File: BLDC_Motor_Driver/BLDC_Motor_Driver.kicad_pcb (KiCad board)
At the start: 4 copper layers, 139 parts, among them J101 Conn_01x08, J102 395221002, J103 USB4105-GF-A, J104 Conn_01x05, J105 Conn_01x05, J106 Conn_01x04, J107 395221005, J108 395221003, J109 Conn_02x12_Counter_Clockwise, J110 395221005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

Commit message: move elements to logical regions
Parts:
- J101: value Conn_01x08 -> Conn_01x10; footprint Connector_PinHeader_2.54mm:PinHeader_1x08_P2.54mm_Vertical -> Connector_PinHeader_2.54mm:PinHeader_1x10_P2.54mm_Vertical
- U302: footprint Package_SO:HSOP-8-1EP_3.9x4.9mm_P1.27mm_EP2.41x3.1mm -> Package_SO:HSOP-8-1EP_3.9x4.9mm_P1.27mm_EP2.41x3.1mm_ThermalVias
- moved J107 249.3 mm to (273.0, 77.5), turned to 90 degrees
- moved C101 241.6 mm to (267.6, 77.7), turned to 180 degrees
- moved C308 229.4 mm to (250.1, 137.9), turned to 180 degrees
- moved C307 229.3 mm to (252.0, 50.0), turned to 180 degrees
- moved J108 219.3 mm to (273.0, 104.0), turned to 90 degrees
- moved D302 217.4 mm to (248.0, 34.5), turned to 180 degrees
- moved J102 203.9 mm to (250.5, 27.0), turned to 180 degrees
- moved J110 200.3 mm to (193.5, 150.0)
- moved C103 190.3 mm to (193.5, 144.9), turned to 90 degrees
- moved C504 185.6 mm to (261.6, 96.4)
- moved C502 185.2 mm to (261.6, 92.9)
- moved C702 180.1 mm to (250.1, 122.9)
- moved C703 180.1 mm to (250.9, 119.6)
- moved C704 180.1 mm to (250.1, 125.5)
- moved C701 180.1 mm to (254.3, 123.2)
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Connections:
- J101 pad 2: /Gate-Driver/GPIO0 -> /Gate-Driver/ENC_B
- J101 pad 3: /Gate-Driver/GPIO1 -> /Gate-Driver/ENC_N
- J101 pad 4: /Gate-Driver/GPIO5 -> /Gate-Driver/GPIO0
- J101 pad 5: /Gate-Driver/GPIO15 -> /Gate-Driver/GPIO1
- J101 pad 6: /Gate-Driver/GPIO16 -> /Gate-Driver/GPIO5
- J101 pad 7: /Gate-Driver/GPIO17 -> /Gate-Driver/GPIO15
- J101 pad 8: /Gate-Driver/GPIO18 -> /Gate-Driver/GPIO16
- J103 pad A6: /D- -> /D+
- J103 pad A7: /D+ -> /D-
- J103 pad B6: /D- -> /D+
- J103 pad B7: /D+ -> /D-
- U101 pad 1: /USB_D+ -> /D+
- U101 pad 2: /USB_D- -> /D-
- U101 pad 5: /D- -> /USB_D-
- U101 pad 6: /D+ -> /USB_D+

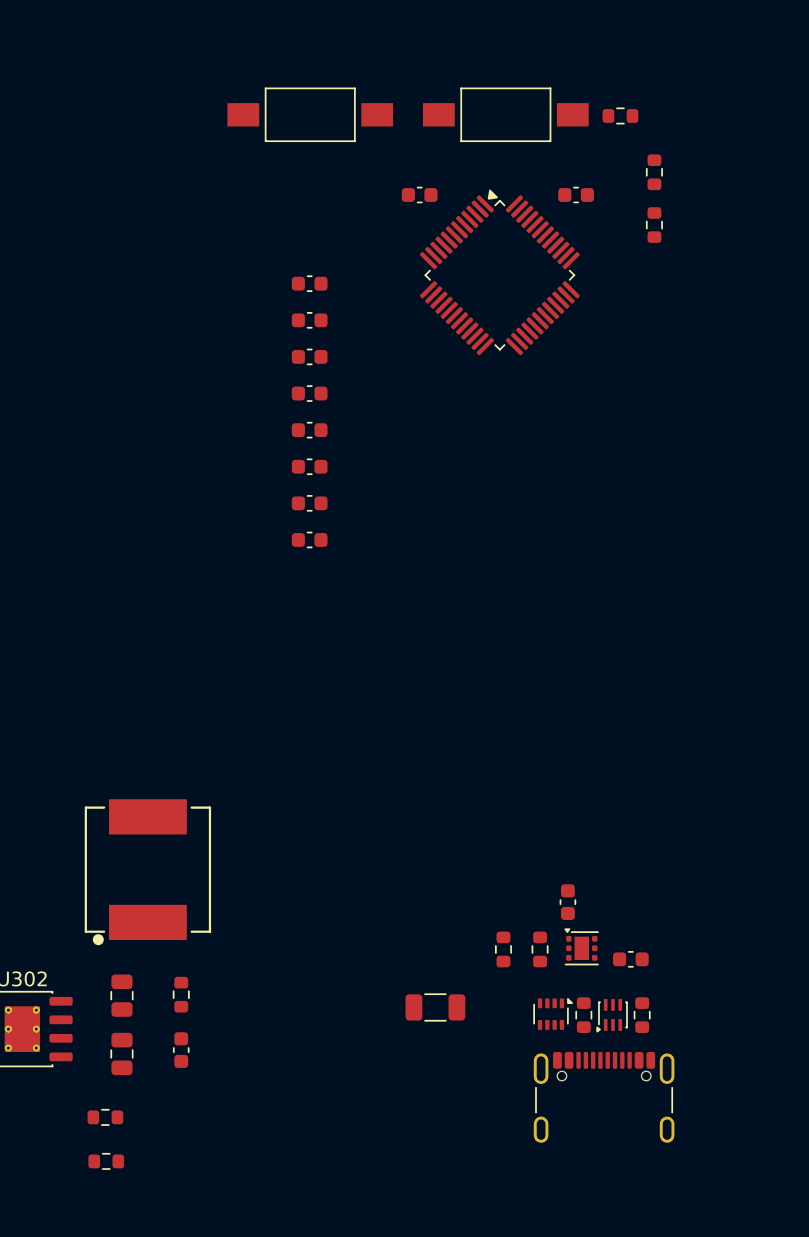
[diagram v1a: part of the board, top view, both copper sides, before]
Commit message: aligned MCU and USB components
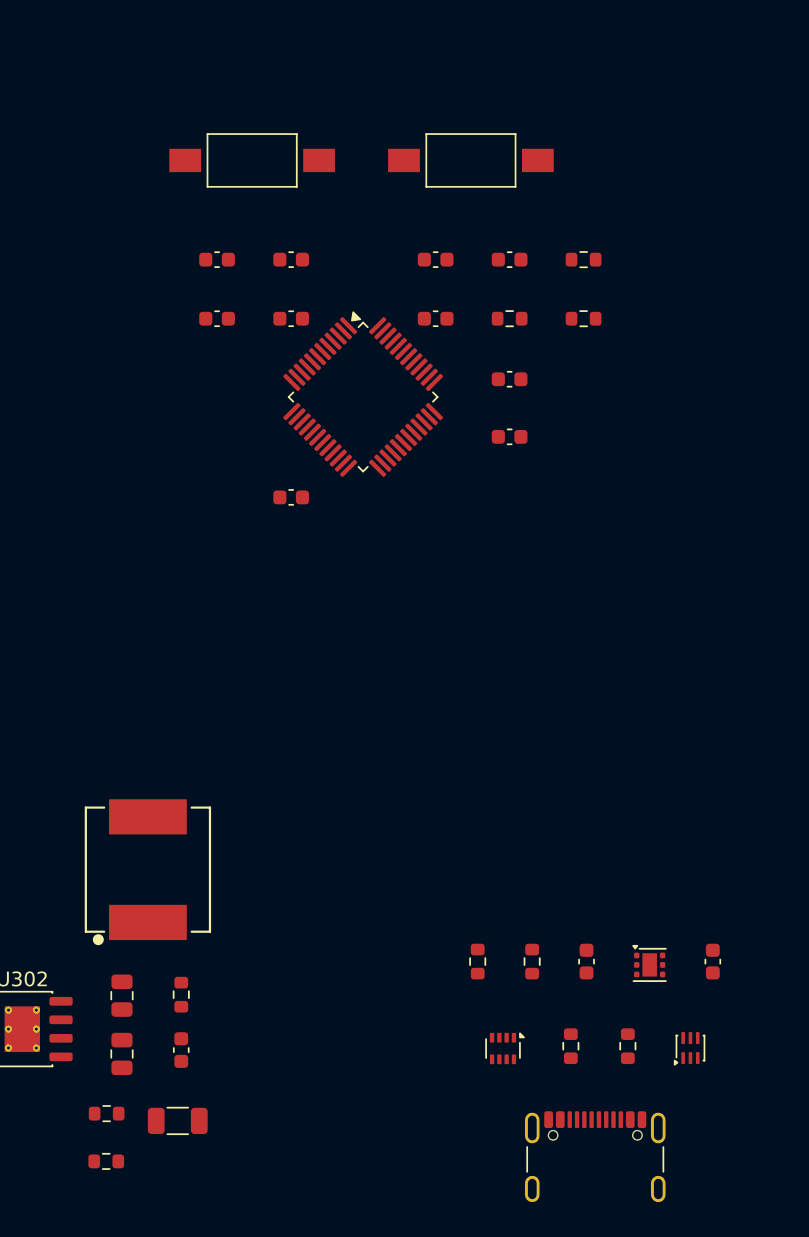
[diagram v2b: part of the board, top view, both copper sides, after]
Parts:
- moved C208 21.1 mm to (148.8, 96.3)
- moved C309 19.3 mm to (131.2, 155.4)
- moved C207 14.4 mm to (153.9, 108.5)
- moved R401 14.1 mm to (153.9, 100.4), turned to 180 degrees
- moved C204 13.7 mm to (153.9, 104.5)
- moved U201 12.6 mm to (143.9, 105.8)
- moved C104 12.2 mm to (138.9, 100.4)
- moved C202 12.2 mm to (138.9, 112.7), turned to 180 degrees
- moved C206 12.0 mm to (133.8, 100.4), turned to 180 degrees
- moved C205 11.8 mm to (138.9, 96.3), turned to 180 degrees
- moved R107 10.2 mm to (159.0, 96.3)
- moved C203 9.02 mm to (148.8, 100.4)
- moved R402 8.05 mm to (159.0, 100.4), turned to 180 degrees
- moved C201 6.56 mm to (133.8, 96.3), turned to 180 degrees
- moved C102 6.36 mm to (153.9, 96.3)
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
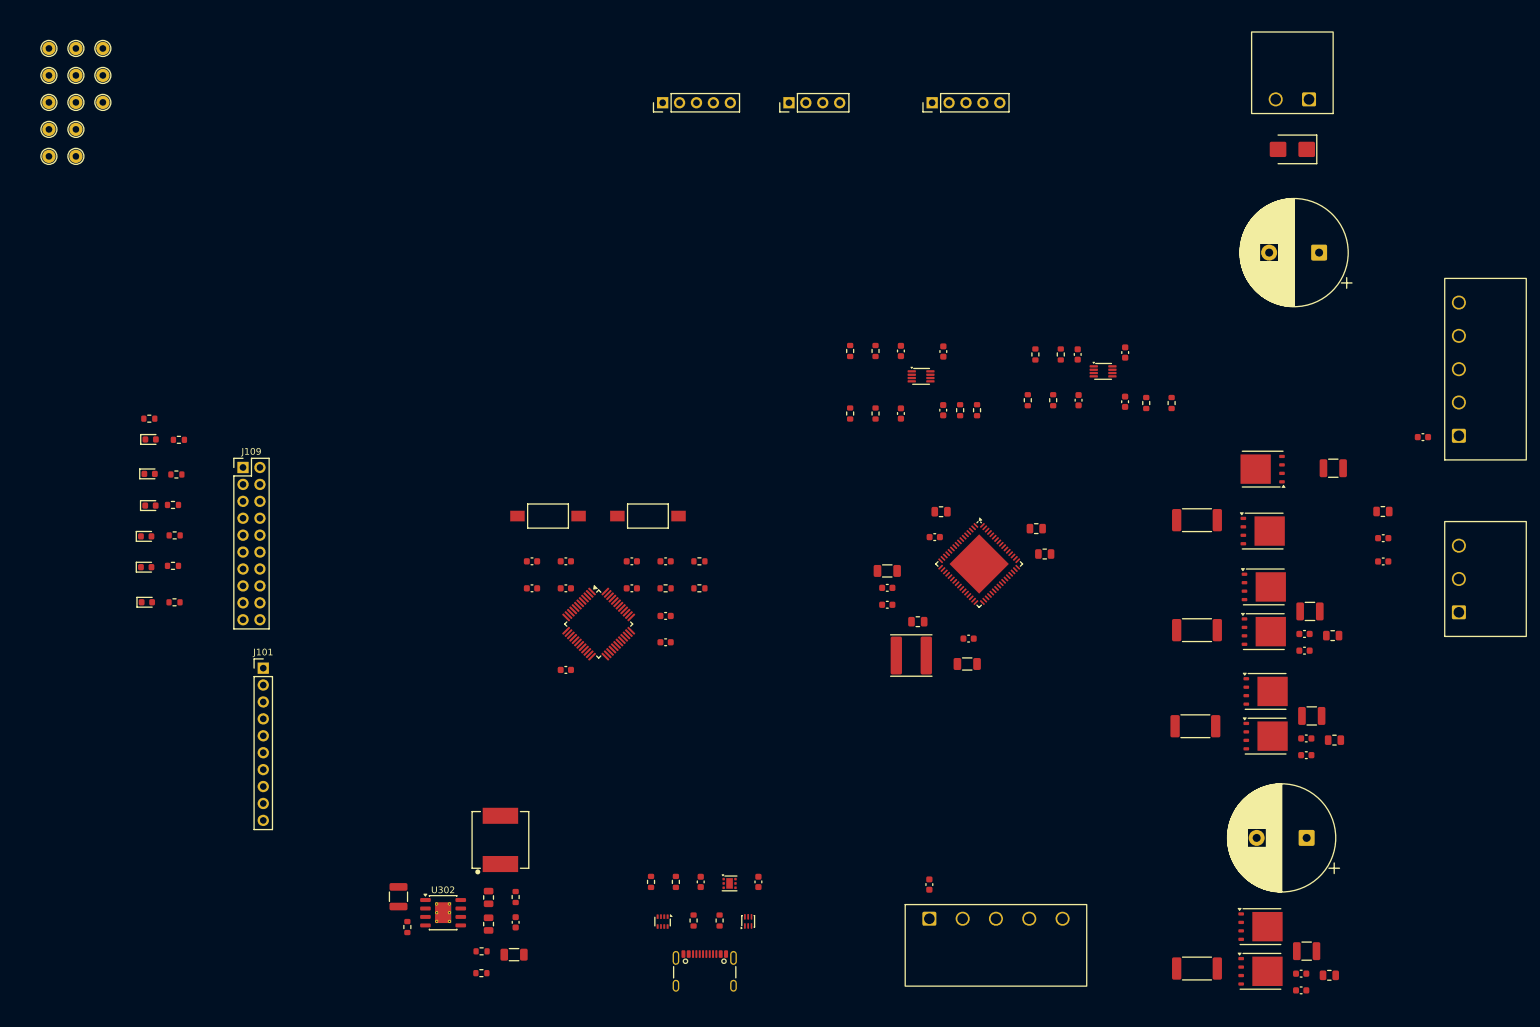
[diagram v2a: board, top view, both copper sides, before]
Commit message: complete top-layer routing for MCU, G_DRV, USB_PWR, HALL areas
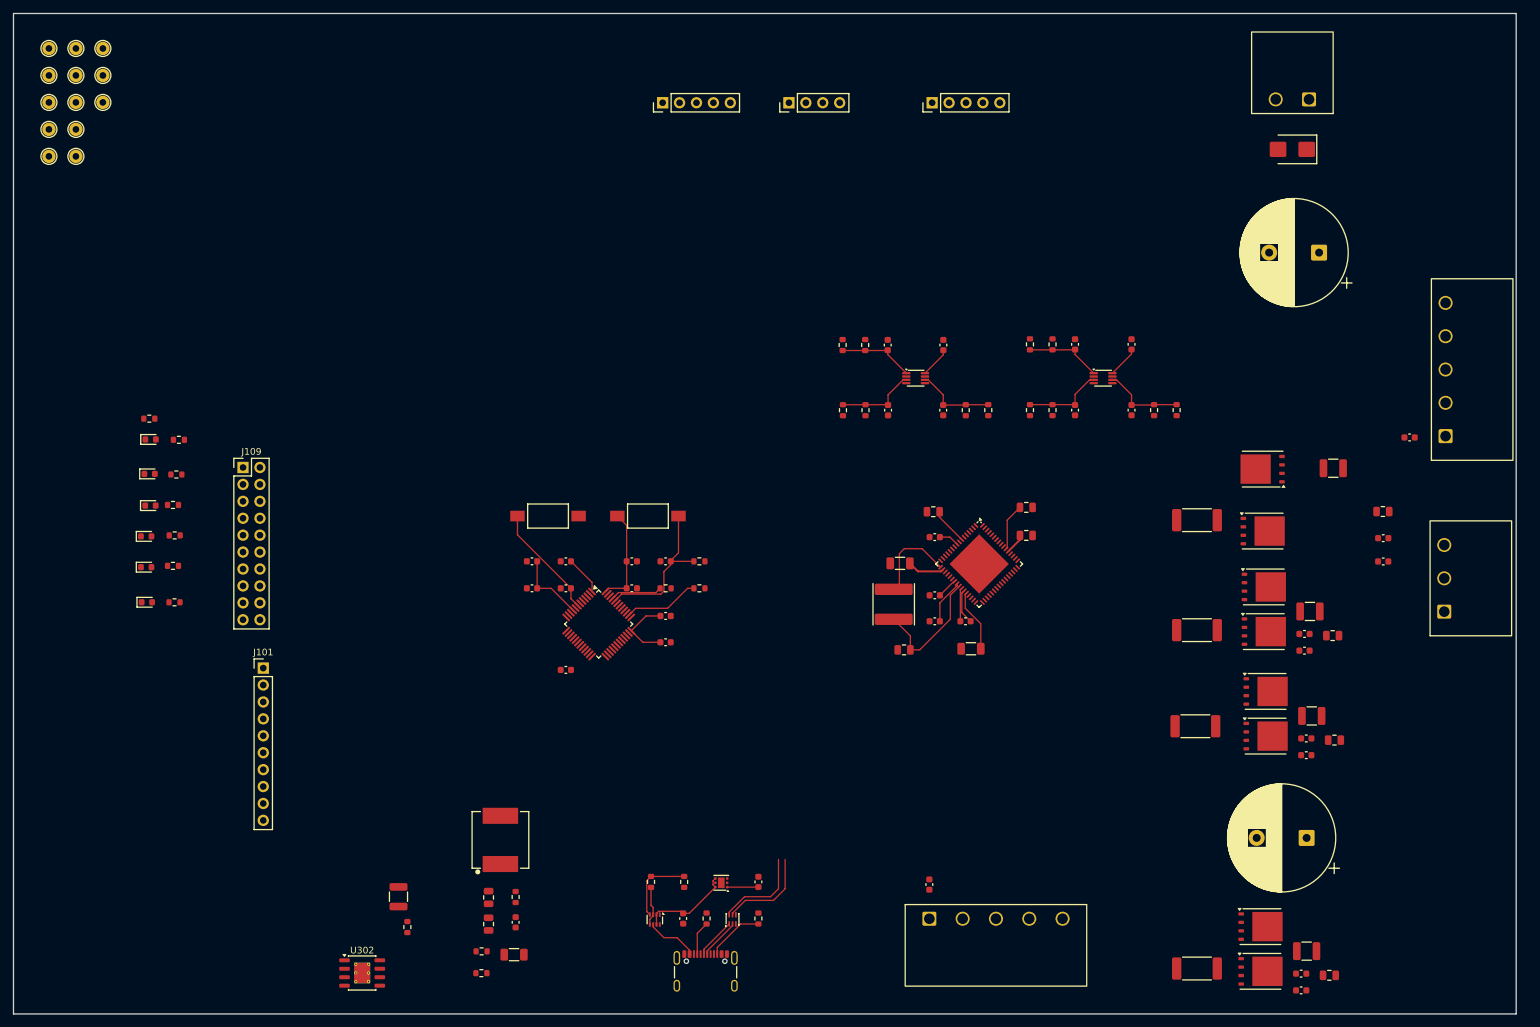
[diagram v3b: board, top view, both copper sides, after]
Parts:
- moved U302 15.2 mm to (108.3, 158.2)
- moved C302 12.6 mm to (156.5, 150.0), turned to -90 degrees
- moved C303 8.66 mm to (167.8, 144.5)
- moved L401 8.13 mm to (188.2, 102.8), turned to -90 degrees
- moved C410 7.54 mm to (194.3, 105.3)
- moved C409 7.21 mm to (194.3, 101.5)
- moved R106 5.83 mm to (167.8, 150.0)
- moved C402 4.71 mm to (189.7, 109.6)
- moved C405 3.93 mm to (208.1, 92.5)
- moved C407 3.53 mm to (208.1, 88.2)
- moved C401 2.64 mm to (198.9, 105.3)
- moved U101 2.37 mm to (164.0, 150.1)
- moved C408 2.36 mm to (199.7, 109.5)
- moved C406 2.23 mm to (189.1, 96.7)
- moved J108 2.20 mm to (270.8, 103.9)
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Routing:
- net +3V3: track 0.00 -> 49.6 mm
- net /BOOT0: track 0.00 -> 23.6 mm
- net /DRIVER_V_{BUCK}: track 0.00 -> 19.1 mm
- net /NRST: track 0.00 -> 17.2 mm
- net /USB_D-: track 0.00 -> 14.1 mm
- net /5V_COM: track 0.00 -> 14.0 mm
- net /USB_D+: track 0.00 -> 13.7 mm
- net /Gate-Driver/DRIVER_SW: track 0.00 -> 13.4 mm
- net /5V_DRV: track 0.00 -> 12.4 mm
- net Net-(U402-3A): track 0.00 -> 12.1 mm
- net Net-(U402-2A): track 0.00 -> 12.1 mm
- net Net-(U403-3A): track 0.00 -> 12.0 mm
- net Net-(U403-2A): track 0.00 -> 12.0 mm
- net Net-(U402-1A): track 0.00 -> 11.9 mm
- net /DRIVER_RSTN: track 0.00 -> 11.4 mm
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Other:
- board outline added: 225.6 x 150.2 mm

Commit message: used external tool to duplicate half-bridge layouts. updated gitignore. redoing gate driver layout with high-side mosfet bootstrap caps
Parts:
- removed C801: 100nF, Capacitor_SMD:C_0805_2012Metric
- removed C802: 1nF, Capacitor_SMD:C_0603_1608Metric
- removed C803: 4.7uF, Capacitor_SMD:C_1210_3225Metric
- removed C804: 1uF, Capacitor_SMD:C_0603_1608Metric
- removed Q801, Q802: CSD18540Q5B, Package_TO_SOT_SMD:TDSON-8-1
- removed R801: 3mΩ, Resistor_SMD:R_2512_6332Metric_Pad1.40x3.35mm_HandSolder
- moved C504 52.6 mm to (209.2, 92.7)
- moved C704 46.2 mm to (209.3, 103.7), turned to 180 degrees
- moved C604 41.7 mm to (209.3, 99.9), turned to 180 degrees
- moved C701 32.2 mm to (224.1, 112.1)
- moved C703 29.3 mm to (223.5, 109.3)
- moved C307 25.7 mm to (263.5, 27.0), turned to 0 degrees
- moved C501 20.7 mm to (241.7, 83.2)
- moved Q701 19.9 mm to (224.3, 119.1), turned to 180 degrees
- moved R501 17.0 mm to (247.7, 80.7)
- moved R601 16.2 mm to (248.3, 99.6)
- moved C702 14.9 mm to (236.6, 116.6), turned to 90 degrees
- moved C503 13.2 mm to (241.1, 80.3)
- moved C601 13.0 mm to (242.2, 102.1)
- moved Q702 12.1 mm to (232.6, 118.7), turned to -90 degrees
- moved R701 12.0 mm to (230.2, 109.6)
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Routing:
- net /DRIVER_V_{BUCK}: track 19.1 -> 0.00 mm
- net GND: track 0.00 -> 18.8 mm
- net /Gate-Driver/DRIVER_SW: track 13.4 -> 0.00 mm
- net /Gate-Driver/DRIVER_V_{DRV}: track 9.39 -> 0.00 mm
- net /Gate-Driver/BS_W: track 0.00 -> 7.65 mm
- net /DRIVER_V_{EXT2}: track 6.71 -> 0.00 mm
- net /Gate-Driver/BS_V: track 0.00 -> 6.59 mm
- net /MOTOR_W: track 0.00 -> 6.52 mm
- net /Gate-Driver/CSP_U: track 0.00 -> 5.59 mm
- net /Gate-Driver/CSP_W: track 0.00 -> 5.59 mm
- net /Gate-Driver/CSP_V: track 0.00 -> 5.59 mm
- net +1V8: track 5.56 -> 0.00 mm
- net /Gate-Driver/DRIVER_CPI: track 5.27 -> 0.00 mm
- net /Gate-Driver/DRIVER_CPO: track 5.03 -> 0.00 mm
- net /MOTOR_U: track 0.00 -> 4.88 mm
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- added copper zone on F.Cu, net (none)
- added copper zone on F.Cu, net +36V
- added copper zone on F.Cu, net /Gate-Driver/CSP_U
- added copper zone on F.Cu, net /Gate-Driver/CSP_V
- added copper zone on F.Cu, net /Gate-Driver/CSP_W
- added copper zone on F.Cu, net /MOTOR_U
- added copper zone on F.Cu, net /MOTOR_V
- added copper zone on F.Cu, net /MOTOR_W
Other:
- board text added: "Gate Driver (G_DRV) Area"
- board text added: "Hall/ENC Input Area"
- board text added: "Kelvin Connection: must be parallel to G_DRV"
- board text added: "MCU Area"
- board text added: "USB_PWR"

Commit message: Finished sub-hierarchy layouts
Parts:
- D301: value RED LED -> 3.3V_LED
- D401: value ORANGE_LED -> FAULT_LED
- moved J103 144.9 mm to (125.3, 18.3), turned to 180 degrees
- moved R106 132.6 mm to (117.4, 27.3), turned to -90 degrees
- moved U101 130.1 mm to (121.3, 27.2), turned to -90 degrees
- moved R105 127.5 mm to (125.2, 27.3), turned to -90 degrees
- moved C302 125.8 mm to (128.7, 27.3), turned to 90 degrees
- moved U303 124.5 mm to (132.9, 27.1), turned to 90 degrees
- moved C303 122.5 mm to (117.4, 32.8), turned to -90 degrees
- moved U301 118.6 mm to (123.0, 32.7), turned to 0 degrees
- moved R307 115.2 mm to (128.5, 32.8), turned to 90 degrees
- moved R306 113.2 mm to (133.5, 32.8), turned to -90 degrees
- moved C203 56.5 mm to (117.0, 53.7), turned to 180 degrees
- moved C104 50.4 mm to (112.1, 57.7)
- moved C205 50.4 mm to (112.1, 53.7)
- moved C206 50.4 mm to (107.0, 57.7)
- moved C207 50.4 mm to (127.0, 65.8)
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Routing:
- net Net-(U302-FB): track 0.00 -> 29.8 mm
- net Net-(U302-SW): track 0.00 -> 18.9 mm
- net /5V_REG: track 5.91 -> 22.8 mm
- net /DRIVER_V_{BUCK}: track 0.00 -> 16.2 mm
- net /Gate-Driver/DRIVER_SW: track 0.00 -> 14.0 mm
- net Net-(C305-Pad1): track 0.00 -> 12.5 mm
- net Net-(U402-3A): track 12.1 -> 0.00 mm
- net Net-(U402-2A): track 12.1 -> 0.00 mm
- net Net-(U403-3A): track 12.0 -> 0.00 mm
- net Net-(U403-2A): track 12.0 -> 0.00 mm
- net Net-(U402-1A): track 11.9 -> 0.00 mm
- net Net-(U403-1A): track 11.4 -> 0.00 mm
- net +3V3: track 46.6 -> 56.3 mm
- net /Gate-Driver/DRIVER_V_{DRV}: track 0.00 -> 7.14 mm
- net +1V8: track 0.00 -> 6.48 mm
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- added copper zone on F.Cu, net GND
- added copper zone on F.Cu, net Net-(U302-RON)
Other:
- board text added: "+36 -> +5"
- board text added: "Inductor Loop not ideal for VBuck. consider redo"
- board text added: "Status LEDs"
- board text added: "User LEDs"
